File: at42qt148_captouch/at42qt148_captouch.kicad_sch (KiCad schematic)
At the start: 43 parts, among them IC1 AT42QT1481-ANR, Y1 WE_XTAL_830011263_16MHZ

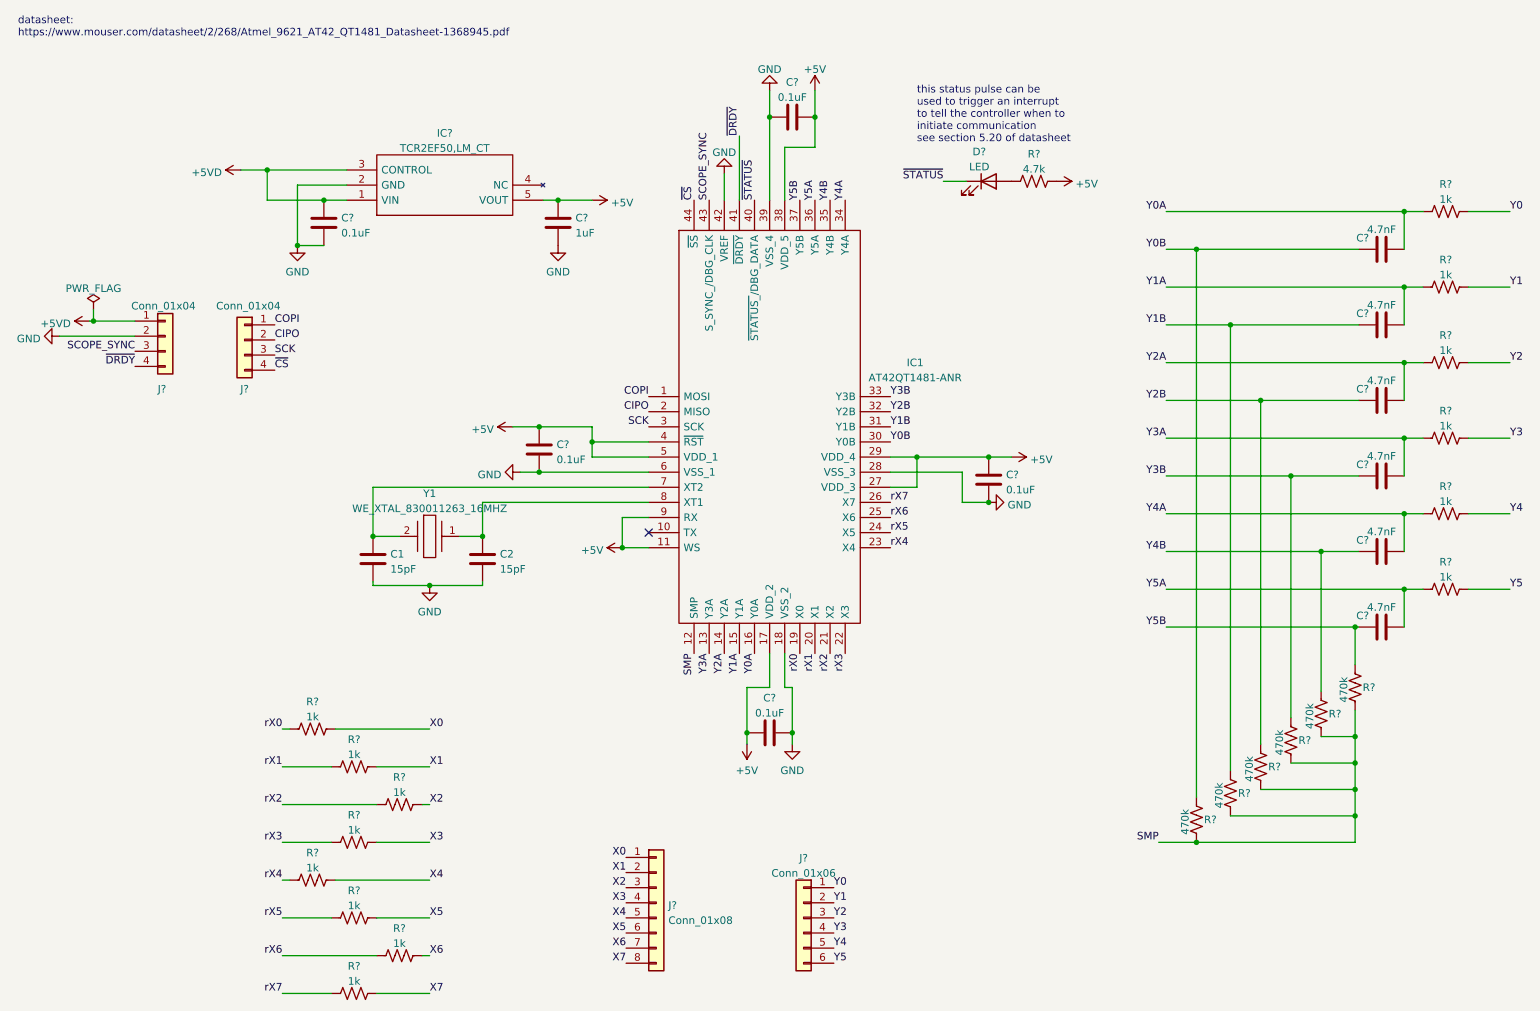
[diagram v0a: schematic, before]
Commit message: almost complete at42qt pcb layout
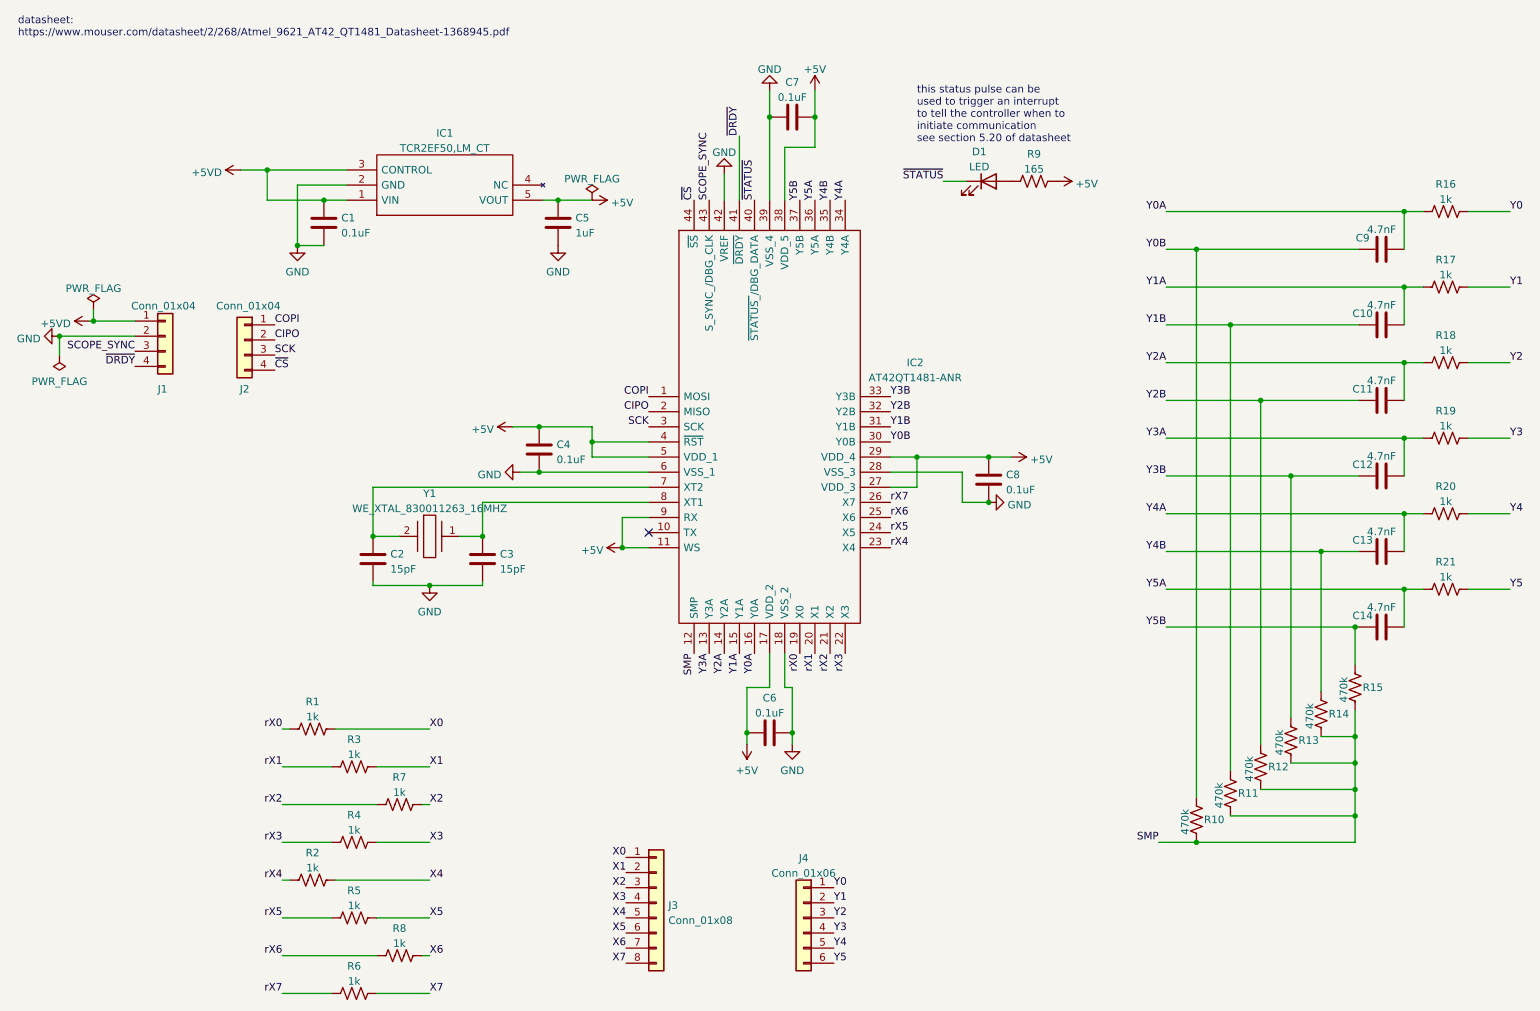
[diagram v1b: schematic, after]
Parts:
- C1, C10, C11, C12, C13, C14, C4, C5, C6, C7, C8, C9: renamed from C?; footprint (none) -> Capacitor_SMD:C_0603_1608Metric
- D1: renamed from D?; footprint (none) -> LED_SMD:LED_0603_1608Metric
- IC1: renamed from IC?; footprint TCR2EF50LMCT -> ASMR_footprints:TCR2EF50LMCT
- J1, J2: renamed from J?; footprint (none) -> Connector_PinHeader_2.54mm:PinHeader_1x04_P2.54mm_Vertical
- J3: renamed from J?; footprint (none) -> Connector_PinSocket_2.54mm:PinSocket_1x08_P2.54mm_Vertical
- J4: renamed from J?; footprint (none) -> Connector_PinSocket_2.54mm:PinSocket_1x06_P2.54mm_Vertical
- R1, R10, R11, R12, R13, R14, R15, R16, R17, R18, R19, R2, R20, R21, R3, R4, R5, R6, R7, R8: renamed from R?; footprint (none) -> Resistor_SMD:R_0603_1608Metric
- R9: renamed from R?; value 4.7k -> 165; footprint (none) -> Resistor_SMD:R_0603_1608Metric
- renumbered C1 to C2, C2 to C3, IC1 to IC2
